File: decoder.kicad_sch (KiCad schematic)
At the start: 0 parts

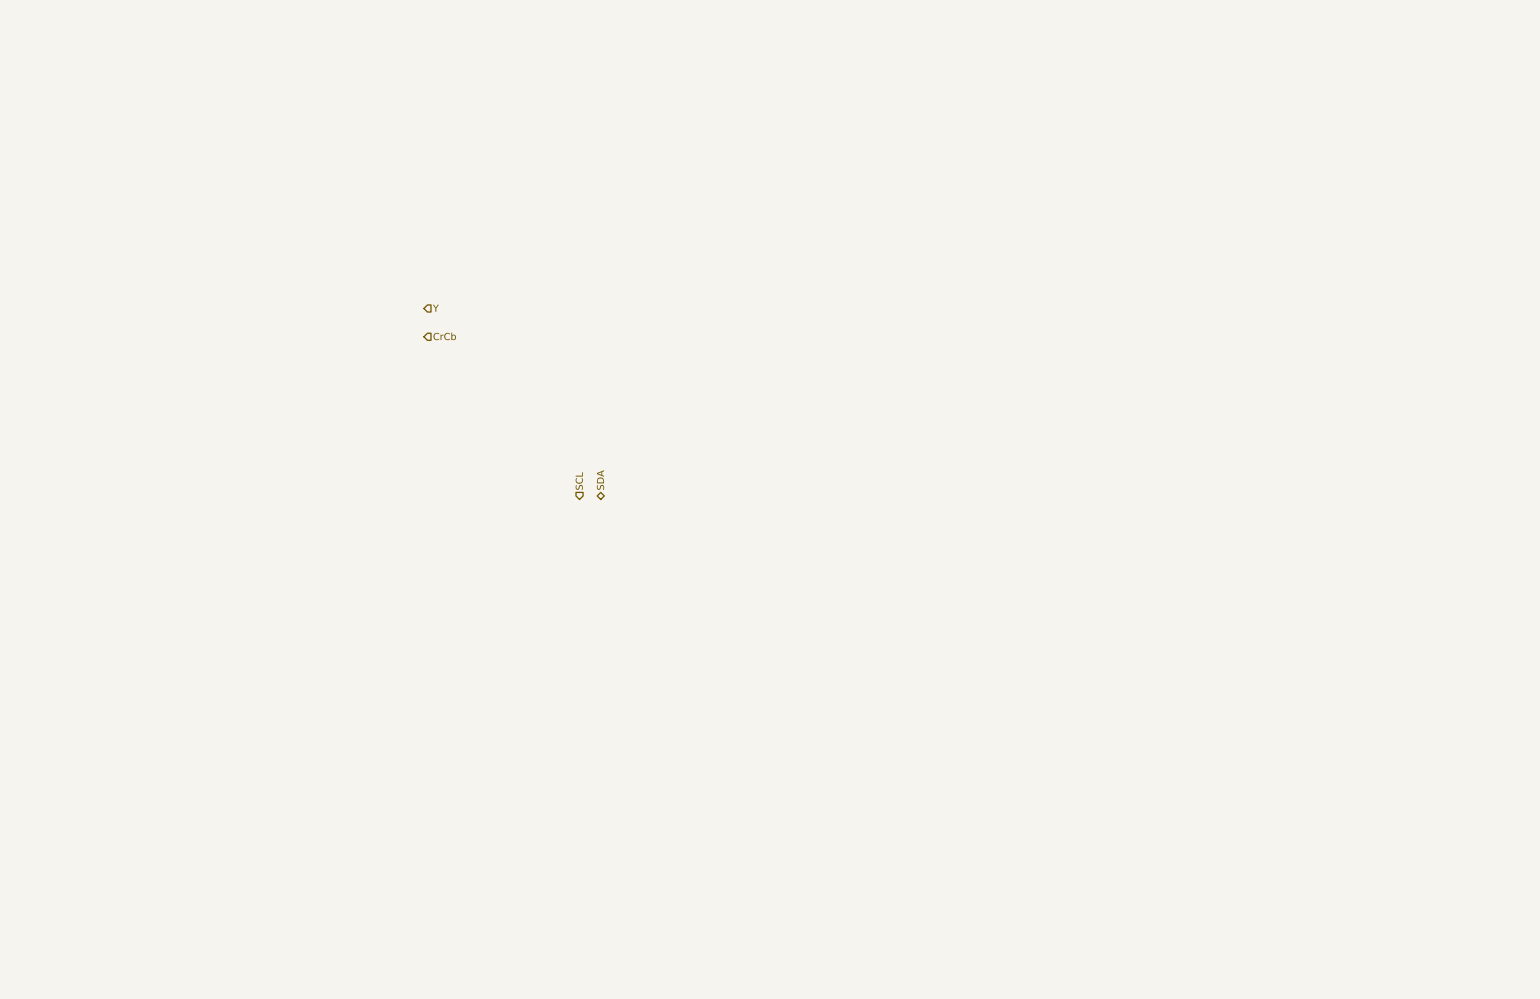
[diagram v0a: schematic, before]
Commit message: continuing schematic capture, renamed sheets
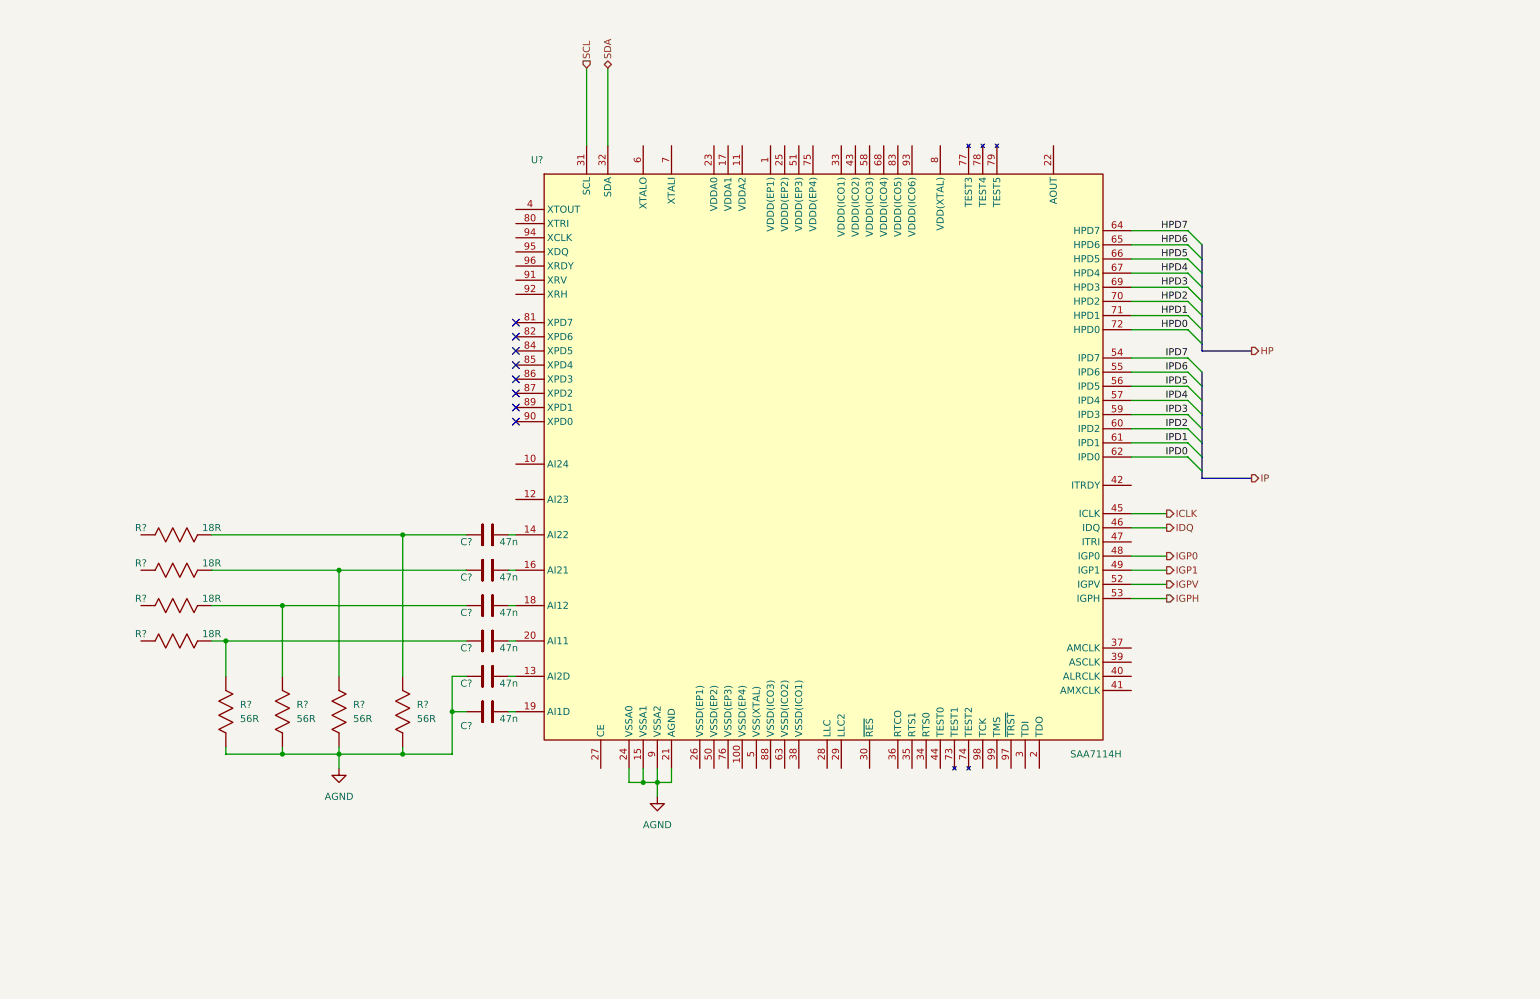
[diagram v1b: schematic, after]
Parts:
- added C? (x6): 47n, symbol tbc:GCJ188R71E473KA01D
- added R? (x4): 18R, symbol tbc:RC0603FR-0718RL
- added R? (x4): 56R, symbol tbc:RC0603FR-0756RL
- added U?: SAA7114H, symbol tbc:SAA7114H
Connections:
- net SCL: now also U?.31 (SCL)
- net SDA: now also U?.32 (SDA)
- new net: C?.1, R?.2, R?.2 (x4)
- new net: C?.2, U?.18 (AI12)
- new net: C?.2, U?.13 (AI2D)
- new net: C?.2, U?.14 (AI22)
- new net: C?.2, U?.16 (AI21)
- new net: C?.2, U?.19 (AI1D)
- new net: C?.2, U?.20 (AI11)
- new net AGND: C?.1, C?.1, R?.1, R?.1, R?.1, R?.1, U?.15 (VSSA1), U?.21 (AGND), U?.24 (VSSA0), U?.9 (VSSA2)
- new net HPD0: U?.72 (HPD0)
- new net HPD1: U?.71 (HPD1)
- new net HPD2: U?.70 (HPD2)
- new net HPD3: U?.69 (HPD3)
- new net HPD4: U?.67 (HPD4)
- new net HPD5: U?.66 (HPD5)
- new net HPD6: U?.65 (HPD6)
- new net HPD7: U?.64 (HPD7)
- new net ICLK: U?.45 (ICLK)
- new net IDQ: U?.46 (IDQ)
- new net IGP0: U?.48 (IGP0)
- new net IGP1: U?.49 (IGP1)
- new net IGPH: U?.53 (IGPH)
- new net IGPV: U?.52 (IGPV)
- new net IPD0: U?.62 (IPD0)
- new net IPD1: U?.61 (IPD1)
- new net IPD2: U?.60 (IPD2)
- new net IPD3: U?.59 (IPD3)
- new net IPD4: U?.57 (IPD4)
- new net IPD5: U?.56 (IPD5)
- new net IPD6: U?.55 (IPD6)
- new net IPD7: U?.54 (IPD7)
- no-connect marks 0 -> 8

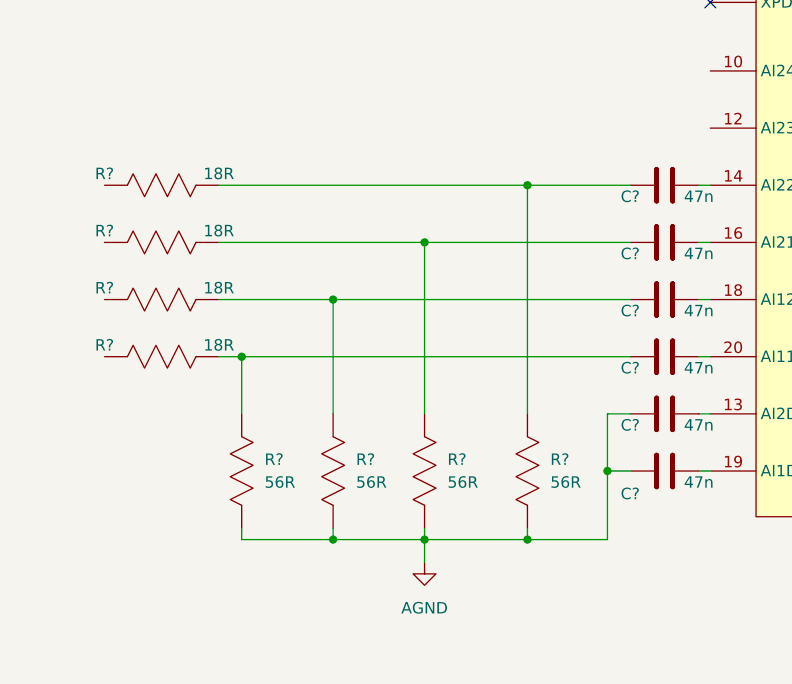
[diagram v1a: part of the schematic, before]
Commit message: added decoder symbol
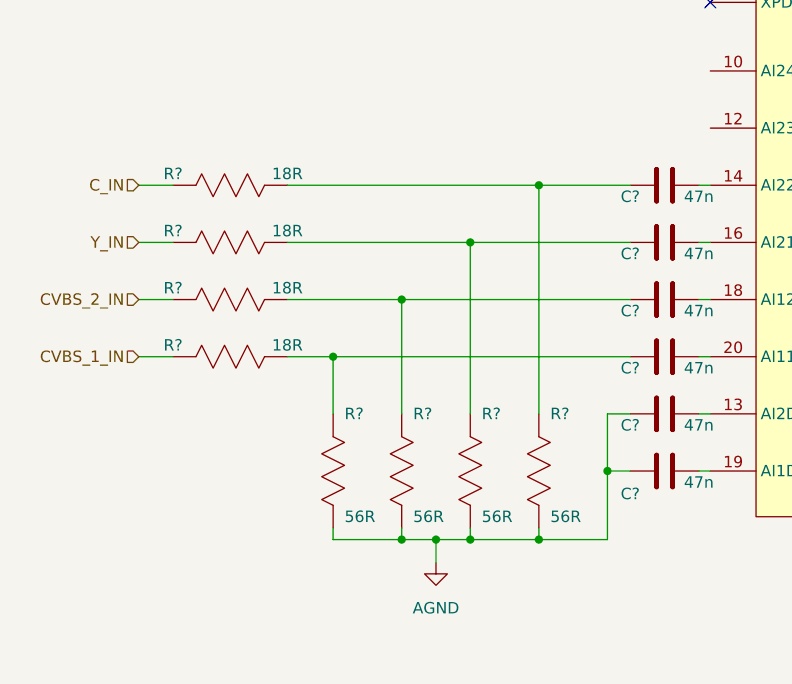
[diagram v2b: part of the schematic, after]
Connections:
- net CVBS_2_IN: now reaches R?.1
- net C_IN: now reaches R?.1
- net Y_IN: now reaches R?.1
- net CVBS_1_IN: now reaches R?.1
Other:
- moved on the sheet: R?
